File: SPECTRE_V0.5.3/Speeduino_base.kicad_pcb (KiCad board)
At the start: 2 copper layers, 100 x 93 mm, 218 parts, among them J1 Conn_01x06_Male, J2 Conn_02x04_Odd_Even, J3 ProtoArea, Q1 AO3400, Q10 BSP78, Q11 BSP78, Q12 AO3400, Q13 BSP78, Q14 BSP78, Q15 BSP78, Q16 BSP78, Q17 BSP78, Q18 BSP78, Q19 BSP78, Q20 BSP78, Q21 BSP78, Q6 AO3400, Q7 AO3400, U1 MAX9926UAEE+, U10 MIC4427, U2 LM78M05_TO220, U3 TL431DBZ, U4 molex_48pin, U5 TJA1050, U6 MAX3232, U7 MIC4427, U8 MIC4427, U9 MIC4427

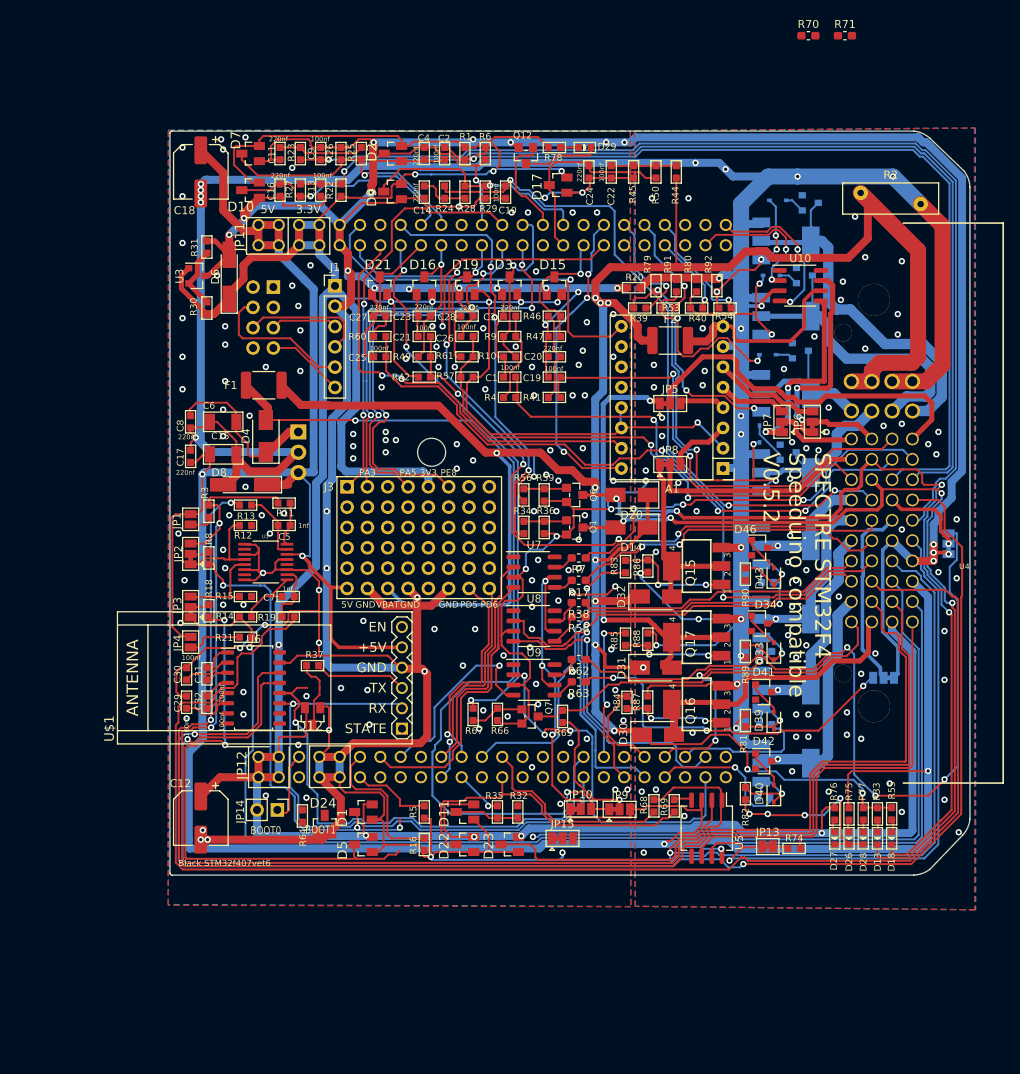
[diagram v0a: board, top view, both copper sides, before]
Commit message: Complete rework on PCB
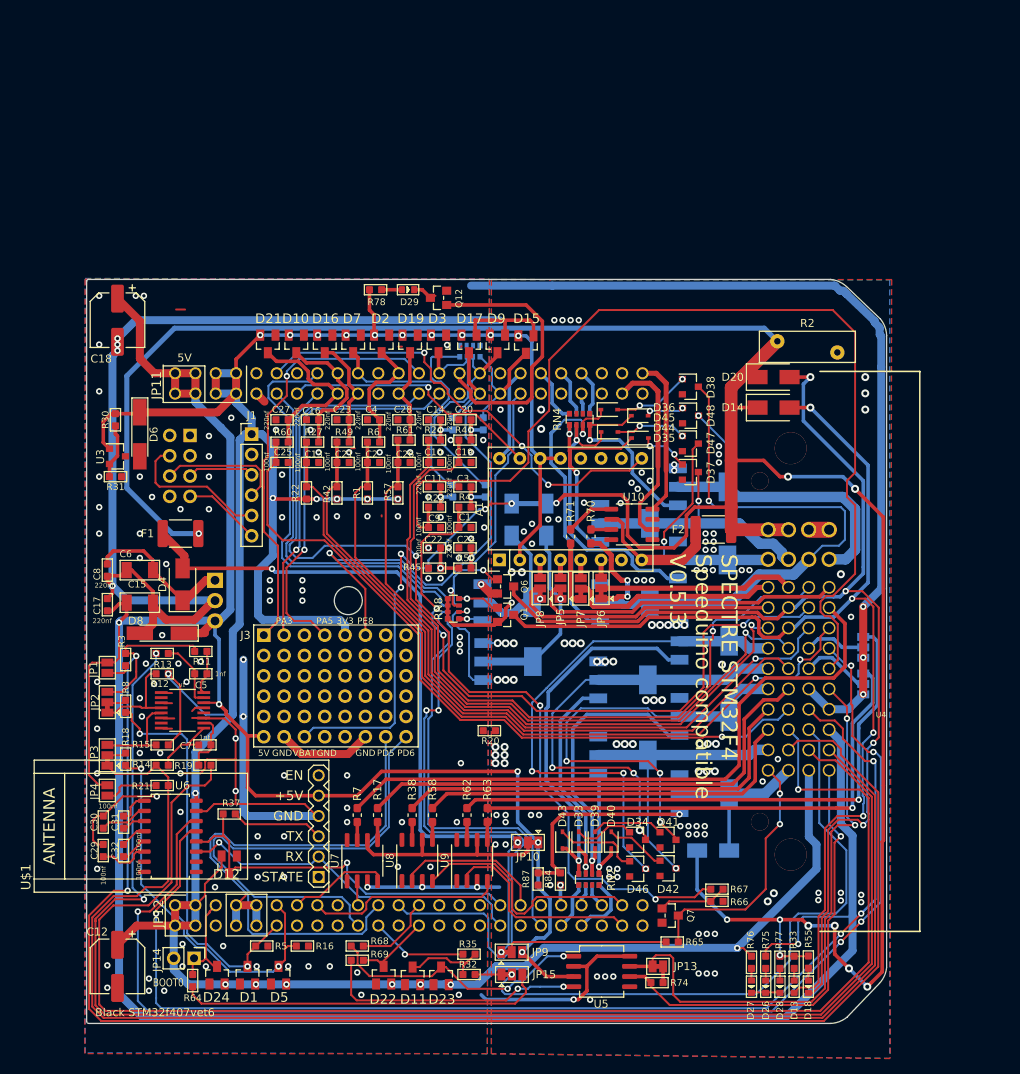
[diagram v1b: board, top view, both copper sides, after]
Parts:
- removed R10, R26, R29, R47: 9k1, Speeduino_base:R0603
- removed R34, R39, R40, R43, R48, R51, R52, R53, R54, R56, R83, R85: 100R, Speeduino_base:R0603
- removed R36, R59, R79, R80, R81, R82, R86, R88, R89, R90, R91, R92: 10k, Speeduino_base:R0603
- added RN1: 100R, Resistor_SMD:R_Array_Convex_4x0612, B.Cu at (166.4, 110.6)
- added RN2: 10K, Resistor_SMD:R_Array_Convex_4x0612, F.Cu at (166.4, 110.6)
- added RN3: 100R, Resistor_SMD:R_Array_Convex_4x0612, B.Cu at (165.2, 53.0)
- added RN4: 10K, Resistor_SMD:R_Array_Convex_4x0612, F.Cu at (165.2, 53.0)
- added RN6: 9K1, Resistor_SMD:R_Array_Convex_4x0612, B.Cu at (151.5, 44.5)
- added RN7: 100R, Resistor_SMD:R_Array_Convex_4x0612, B.Cu at (149.4, 76.7)
- added RN8: 10K, Resistor_SMD:R_Array_Convex_4x0612, F.Cu at (149.4, 76.7)
- D30, D31, D32, Q15, Q16, Q17, R25, R28, R44, R46, R9: moved to B.Cu
- D35, D36, D37, D38, D44, D45, D47, D48: moved to F.Cu
- R66, R87: value 10k -> 10K
- U4: footprint Speeduino_base:Molex_48 -> rusefi_lib:Molex_48
- moved R71 71.4 mm to (164.1, 67.7), turned to 90 degrees
- moved R70 68.2 mm to (166.6, 67.7), turned to 90 degrees
- moved R20 58.2 mm to (153.9, 91.9)
- moved R44 58.0 mm to (147.1, 71.6), turned to 90 degrees
- moved R45 55.4 mm to (147.1, 71.6), turned to 90 degrees
- moved R50 55.0 mm to (150.9, 71.6), turned to 90 degrees
- moved C22 51.9 mm to (147.1, 69.1), turned to 90 degrees
- moved C24 49.5 mm to (150.9, 69.1), turned to 90 degrees
- moved C9 48.9 mm to (147.1, 66.5), turned to 270 degrees
- moved R23 47.3 mm to (147.1, 64.0), turned to 90 degrees
- moved C11 45.9 mm to (147.1, 61.5), turned to 90 degrees
- moved R1 44.1 mm to (138.7, 62.2), turned to 0 degrees
- moved R69 44.1 mm to (137.4, 120.7), turned to 270 degrees
- moved R25 43.7 mm to (149.4, 62.0), turned to 0 degrees
- moved D46 42.9 mm to (172.5, 109.2)
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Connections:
- A1 pad 10: Net-(A1-Pad10) -> (no net)
- A1 pad 11: Net-(A1-Pad11) -> (no net)
- A1 pad 12: Net-(A1-Pad12) -> (no net)
- J2 pad 1: Net-(J2-Pad1) -> (no net)
- J2 pad 2: Net-(J2-Pad2) -> (no net)
- J2 pad 3: Net-(J2-Pad3) -> (no net)
- J2 pad 8: Net-(J2-Pad8) -> (no net)
- J3 pad 10: Net-(J3-Pad10) -> (no net)
- J3 pad 11: Net-(J3-Pad11) -> (no net)
- J3 pad 12: Net-(J3-Pad12) -> (no net)
- J3 pad 13: Net-(J3-Pad13) -> (no net)
- J3 pad 14: Net-(J3-Pad14) -> (no net)
- J3 pad 15: Net-(J3-Pad15) -> (no net)
- J3 pad 16: Net-(J3-Pad16) -> (no net)
- J3 pad 17: Net-(J3-Pad17) -> (no net)
- J3 pad 18: Net-(J3-Pad18) -> (no net)
- J3 pad 19: Net-(J3-Pad19) -> (no net)
- J3 pad 20: Net-(J3-Pad20) -> (no net)
- J3 pad 21: Net-(J3-Pad21) -> (no net)
- J3 pad 22: Net-(J3-Pad22) -> (no net)
- J3 pad 23: Net-(J3-Pad23) -> (no net)
- J3 pad 24: Net-(J3-Pad24) -> (no net)
- J3 pad 25: Net-(J3-Pad25) -> (no net)
- J3 pad 26: Net-(J3-Pad26) -> (no net)
- J3 pad 27: Net-(J3-Pad27) -> (no net)
- J3 pad 28: Net-(J3-Pad28) -> (no net)
- J3 pad 29: Net-(J3-Pad29) -> (no net)
- J3 pad 3: Net-(J3-Pad3) -> (no net)
- J3 pad 30: Net-(J3-Pad30) -> (no net)
- J3 pad 31: Net-(J3-Pad31) -> (no net)
- J3 pad 32: Net-(J3-Pad32) -> (no net)
- J3 pad 33: Net-(J3-Pad33) -> (no net)
- J3 pad 34: Net-(J3-Pad34) -> (no net)
- J3 pad 35: Net-(J3-Pad35) -> (no net)
- J3 pad 36: Net-(J3-Pad36) -> (no net)
- J3 pad 37: Net-(J3-Pad37) -> (no net)
- J3 pad 38: Net-(J3-Pad38) -> (no net)
- J3 pad 39: Net-(J3-Pad39) -> (no net)
- J3 pad 40: Net-(J3-Pad40) -> (no net)
- J3 pad 45: Net-(J3-Pad45) -> (no net)
- J3 pad 7: Net-(J3-Pad7) -> (no net)
- J3 pad 8: Net-(J3-Pad8) -> (no net)
- J3 pad 9: Net-(J3-Pad9) -> (no net)
- JP11 pad 13: PE4 -> (no net)
- JP11 pad 21: Net-(JP11-Pad21) -> (no net)
- JP11 pad 22: Net-(JP11-Pad22) -> (no net)
- JP11 pad 30: Net-(JP11-Pad30) -> (no net)
- JP11 pad 33: Net-(JP11-Pad33) -> (no net)
- JP11 pad 38: PE10 -> (no net)
- JP11 pad 40: PE12 -> (no net)
- JP11 pad 43: PE15 -> (no net)
- JP11 pad 44: PB10 -> (no net)
- JP11 pad 45: PB11 -> (no net)
- JP11 pad 48: PB14 -> (no net)
- JP12 pad 14: PB8 -> (no net)
- JP12 pad 16: PB6 -> (no net)
- JP12 pad 17: PB5 -> (no net)
- JP12 pad 18: PB3 -> (no net)
- JP12 pad 24: Net-(JP12-Pad24) -> (no net)
- JP12 pad 27: Net-(JP12-Pad27) -> (no net)
- JP12 pad 28: Net-(JP12-Pad28) -> (no net)
- JP12 pad 29: Net-(JP12-Pad29) -> (no net)
- JP12 pad 30: Net-(JP12-Pad30) -> (no net)
- JP12 pad 31: Net-(JP12-Pad31) -> (no net)
- JP12 pad 32: Net-(JP12-Pad32) -> (no net)
- JP12 pad 36: Net-(JP12-Pad36) -> (no net)
- JP12 pad 37: PC8 -> (no net)
- JP12 pad 44: PD11 -> (no net)
- JP12 pad 47: PD8 -> (no net)
- JP12 pad 48: PB15 -> (no net)
- JP12 pad 6: BOOT1 -> (no net)
- R74 pad 1: Net-(JP13-Pad1) -> CANL
- R74 pad 2: CANL -> Net-(JP13-Pad1)
- U$1 pad 1: Net-(U$1-Pad1) -> (no net)
- U$1 pad 6: Net-(U$1-Pad6) -> (no net)
- U1 pad 12: Net-(U1-Pad12) -> (no net)
- U1 pad 2: Net-(U1-Pad2) -> (no net)
- U1 pad 7: Net-(U1-Pad7) -> (no net)
- U10 pad 1: Net-(U10-Pad1) -> (no net)
- U10 pad 8: Net-(U10-Pad8) -> (no net)
- U5 pad 5: Net-(U5-Pad5) -> (no net)
- U6 pad 10: Net-(U6-Pad10) -> (no net)
- U6 pad 7: Net-(U6-Pad7) -> (no net)
- U6 pad 8: Net-(U6-Pad8) -> (no net)
- U6 pad 9: Net-(U6-Pad9) -> (no net)
- U7 pad 1: Net-(U7-Pad1) -> (no net)
- U7 pad 8: Net-(U7-Pad8) -> (no net)
- U8 pad 1: Net-(U8-Pad1) -> (no net)
- U8 pad 8: Net-(U8-Pad8) -> (no net)
- U9 pad 1: Net-(U9-Pad1) -> (no net)
- U9 pad 8: Net-(U9-Pad8) -> (no net)
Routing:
- net GND: track 706.9 -> 260.2 mm, vias 158 -> 110
- net PWR_GND: track 455.5 -> 160.8 mm, vias 97 -> 129
- net 3.3V: track 496.5 -> 386.9 mm, vias 14 -> 24
- net VBAT: track 306.6 -> 362.5 mm, vias 12 -> 15
- net PD15: track 60.0 -> 6.03 mm, vias 2 -> 0
- net BOOT0_EXT: track 0.00 -> 46.2 mm
- net INJ4-OUT: track 24.7 -> 66.3 mm, vias 1 -> 3
- net PD5: track 26.6 -> 67.1 mm, vias 1 -> 0
- net PC13: track 69.3 -> 109.8 mm
- net PD3: track 36.4 -> 75.2 mm, vias 1 -> 2
- net Net-(D43-Pad1): track 11.7 -> 48.0 mm
- net PE1: track 85.0 -> 49.3 mm
- net BARO: track 59.1 -> 94.2 mm, vias 2 -> 1
- net PD6: track 27.8 -> 60.5 mm, vias 1 -> 0
- net INJ3-OUT: track 23.1 -> 55.5 mm, vias 1 -> 3
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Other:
- board text added: "SPECTRE STM32F4 Speeduino compatible V0.5.3"
- board text removed: "3.3V"
- board text removed: "BOOT1"
- board text removed: "SPECTRE STM32F4 Speeduino compatible V0.5.2"
